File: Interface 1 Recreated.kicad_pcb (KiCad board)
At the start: 2 copper layers, 222.4 x 72.5 mm, 76 parts, among them Q1 BC213C, Q10 BC183, Q11 BC183, Q2 BC213C, Q3 BC184C, Q4 BC213C, Q5 BC213C, Q6 BC184C, U1 LA15-302, U2 TMS4764, U3 74LS260, U4 74HC04, X1 8Mhz

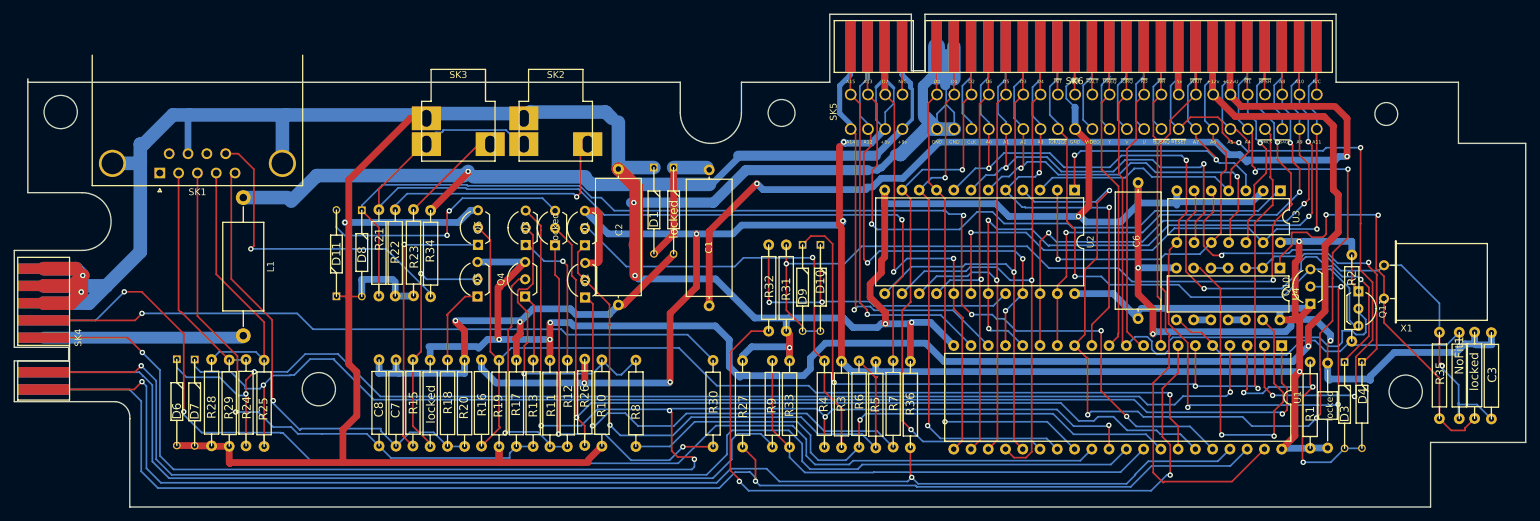
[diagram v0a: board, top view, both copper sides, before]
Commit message: Add files via upload
Updated with Kicad 9. Now includes bom/ibom.html (Interactice BOM)
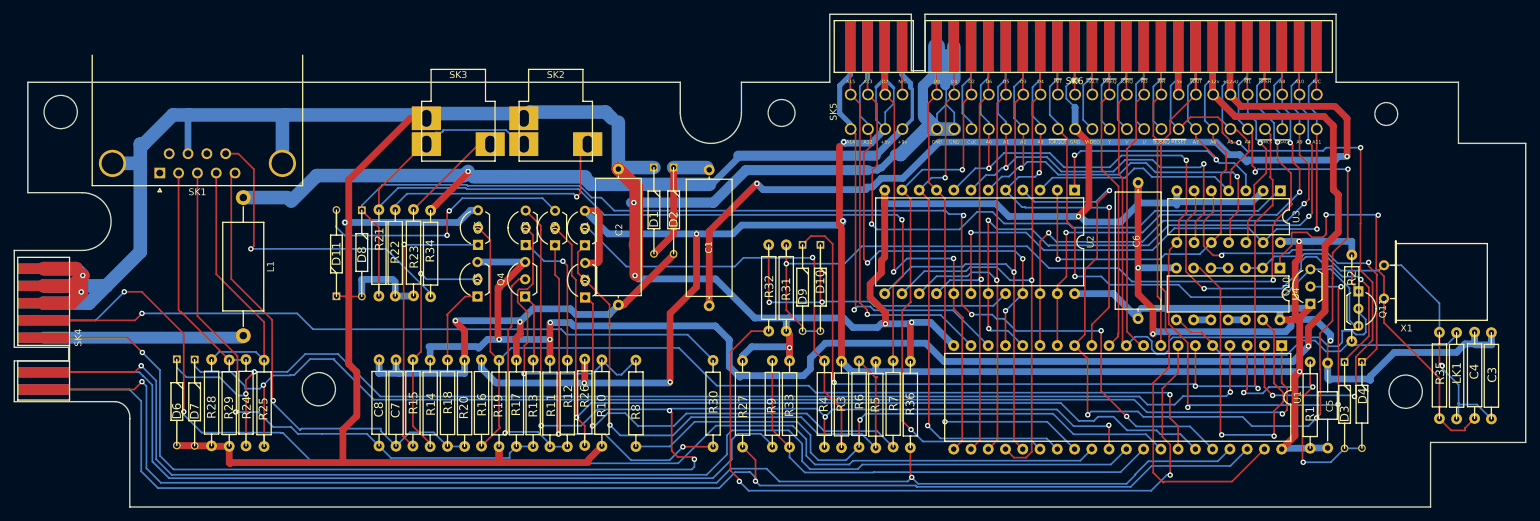
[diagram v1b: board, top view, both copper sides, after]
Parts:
- removed NoFit1: 0R, Spectrum:Resistor_0.25W
- added LK1: 0R, Mod:Resistor_0.25W, F.Cu at (255.2, 103.8)
- C1, C2, C6: footprint Capacitor_THT:C_Axial_L17.0mm_D6.5mm_P20.00mm_Horizontal -> Mod:C_Axial_L17.0mm_D6.5mm_P20.00mm_Horizontal
- C3, C7, C8: footprint Spectrum:Capacitor Ceramic -> Mod:Capacitor Ceramic
- C4: renamed from locked; footprint Spectrum:Capacitor Ceramic -> Mod:Capacitor Ceramic
- C5: renamed from locked; footprint Capacitor_THT:C_Axial_L3.8mm_D2.6mm_P12.50mm_Horizontal -> Mod:C_Axial_L3.8mm_D2.6mm_P12.50mm_Horizontal
- D1, D10, D11, D3, D4, D6, D7, D8, D9: footprint Spectrum:Diode 1N -> Mod:Diode 1N
- D2: renamed from locked; footprint Spectrum:Diode 1N -> Mod:Diode 1N
- L1: footprint Inductor_THT:L_Axial_L12.8mm_D5.8mm_P20.32mm_Horizontal_Fastron_HBCC -> Mod:L_Axial_L12.8mm_D5.8mm_P20.32mm_Horizontal_Fastron_HBCC
- Q1, Q10, Q11, Q2, Q3, Q4, Q5, Q6: footprint Package_TO_SOT_THT:TO-92L_Inline_Wide -> Mod:TO-92L_Inline_Wide
- Q9: renamed from locked; footprint Package_TO_SOT_THT:TO-92L_Inline_Wide -> Mod:TO-92L_Inline_Wide
- R1: footprint ZX Bits:Resistor_0.25W -> Mod:Resistor_0.25W
- R10, R11, R12, R13, R15, R16, R17, R18, R19, R20, R21, R22, R23, R24, R25, R26, R27, R28, R29, R3, R30, R31, R32, R33, R34, R35, R36, R4, R5, R6, R7, R8, R9: footprint Spectrum:Resistor_0.25W -> Mod:Resistor_0.25W
- R14: renamed from locked; footprint Spectrum:Resistor_0.25W -> Mod:Resistor_0.25W
- R2: value NoFit -> 10K; footprint Spectrum:Resistor_0.25W -> Mod:Resistor_0.25W
- SK1: footprint Connector_Dsub:DSUB-9_Female_Horizontal_P2.77x2.84mm_EdgePinOffset14.56mm_Housed_MountingHolesOffset15.98mm -> Mod:DSUB-9_Female_Horizontal_P2.77x2.84mm_EdgePinOffset14.56mm_Housed_MountingHolesOffset15.98mm
- SK2, SK3: footprint ZX Spectrum 3.5mm:ZX Spectrum 3.5mm Skt -> Mod:ZX Spectrum 3.5mm Skt
- SK4: footprint ZX Bits:ZX_MD_Edge_Connector -> Mod:ZX_MD_Edge_Connector
- SK5: footprint ZX Bits:Spectrum_Edge_Connector -> Mod:Edge_Connector_Up_To_Spectrum
- SK6: footprint ZX Bits:ZX_Bus_Edge_Connector -> Mod:Edge_Connector_To_AddOn
- U1: footprint Package_DIP:DIP-40_W15.24mm -> Mod:DIP-40_W15.24mm
- U2: footprint Package_DIP:DIP-24_W15.24mm -> Mod:DIP-24_W15.24mm
- U3, U4: footprint Package_DIP:DIP-14_W7.62mm -> Mod:DIP-14_W7.62mm
- X1: footprint Crystal:Crystal_HC18-U_Horizontal -> Mod:Crystal_HC18-U_Horizontal
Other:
- outline, holes or cut-outs redrawn
